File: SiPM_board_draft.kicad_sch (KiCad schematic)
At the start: 45 parts, among them J1 Conn_01x01_Pin, J10 Conn_01x01_Pin, J11 Conn_01x01_Pin, J12 Conn_01x01_Pin, J13 Conn_01x01_Pin, J14 Conn_01x01_Pin, J15 Conn_01x01_Pin, J16 Conn_01x01_Pin, J17 Conn_01x01_Pin, J18 Conn_01x01_Pin, J19 Conn_01x01_Pin, J2 Conn_01x01_Pin, J20 Conn_01x01_Pin, J21 Conn_01x01_Pin, J22 Conn_01x01_Pin, J23 Conn_01x01_Pin, J24 Conn_01x01_Pin, J25 Conn_01x01_Pin, J26 Conn_01x01_Pin, J27 Conn_01x01_Pin, J28 Conn_01x01_Pin, J29 Conn_01x01_Pin, J3 Conn_01x01_Pin, J30 Conn_01x01_Pin, J31 Conn_01x01_Pin, J32 Conn_01x01_Pin, J4 Conn_01x01_Pin, J5 Conn_01x01_Pin, J6 Conn_01x01_Pin, J7 Conn_01x01_Pin, J8 Conn_01x01_Pin, J9 Conn_01x01_Pin

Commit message: V1.0 submitted for fab
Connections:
- net A8: now also JP3.3 (B); no longer JP3.2 (C)
- net B3: now also JP2.3 (B); no longer JP2.2 (C)
- net C8: now also JP3.2 (C); no longer JP3.3 (B)
- net D1: now also JP2.2 (C); no longer JP2.3 (B)
- net E1: now also JP5.2 (C); no longer JP5.1 (A)
- net F8: now also JP8.2 (C); no longer JP8.1 (A)
- net G1: now also JP5.1 (A); no longer JP5.2 (C)
- net G5: now also JP7.2 (C); no longer JP7.3 (B)
- net G7: now also JP7.3 (B); no longer JP7.2 (C)
- net H2: now also JP6.3 (B); no longer JP6.2 (C)
- net H4: now also JP6.2 (C); no longer JP6.3 (B)
- net H8: now also JP8.1 (A); no longer JP8.2 (C)
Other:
- note added: "A1+A2+B2"
- note added: "A3+A4+B4"
- note added: "C1+D1+D2"
- note added: "Cable to SiPM connections"
- note added: "D3+D4+C4"
- note added: "SiPM part number: S14161-6050HS-04 Datasheet: https://www.hamamatsu.com/content/dam/hamamatsu-photonics/sites/documents/99_SALES_LIBRARY/ssd/s14160_s14161_series_kapd1064e.pdf"
- note added: "SiPM pinout"
- note added: "SiPM: pinout & ganged channels"
- note added: "Unplated throug-holes for mounting"
- company: (none) -> Lawrence Berkeley National Laboratory
- title: (none) -> QuIPS SiPM breakout board
- moved on the sheet: H1, H2, H3, H4, U1

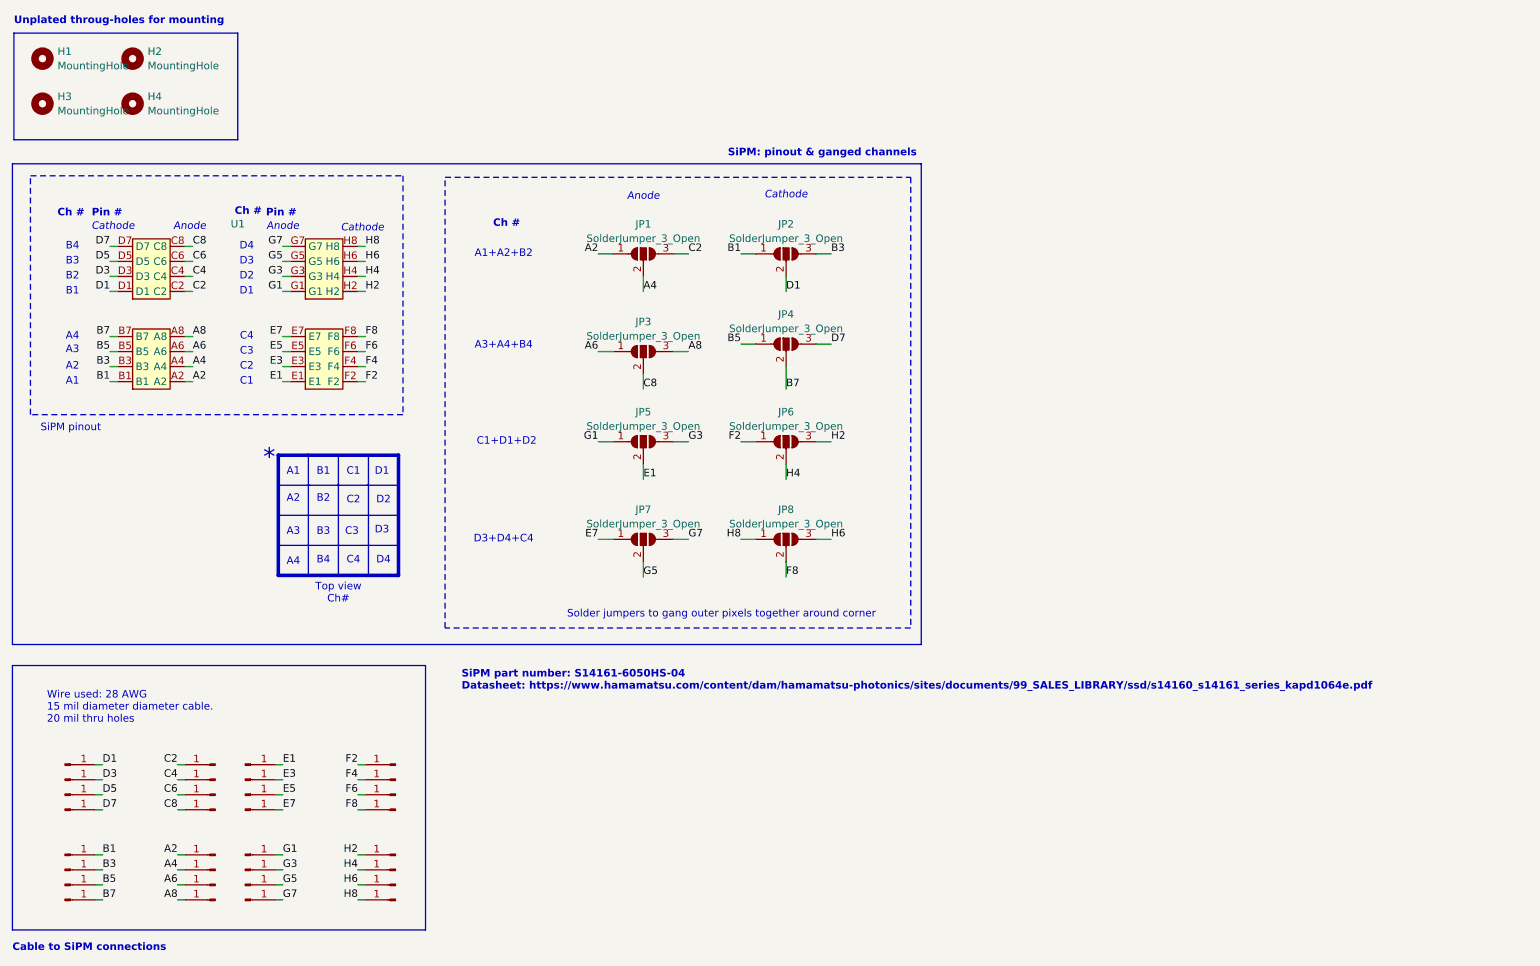
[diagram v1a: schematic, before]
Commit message: First draft of schematic for RC variant of board complete. Started placing with 0402 resistors and 1210 caps. Caps are really big. See if I can go smaller?
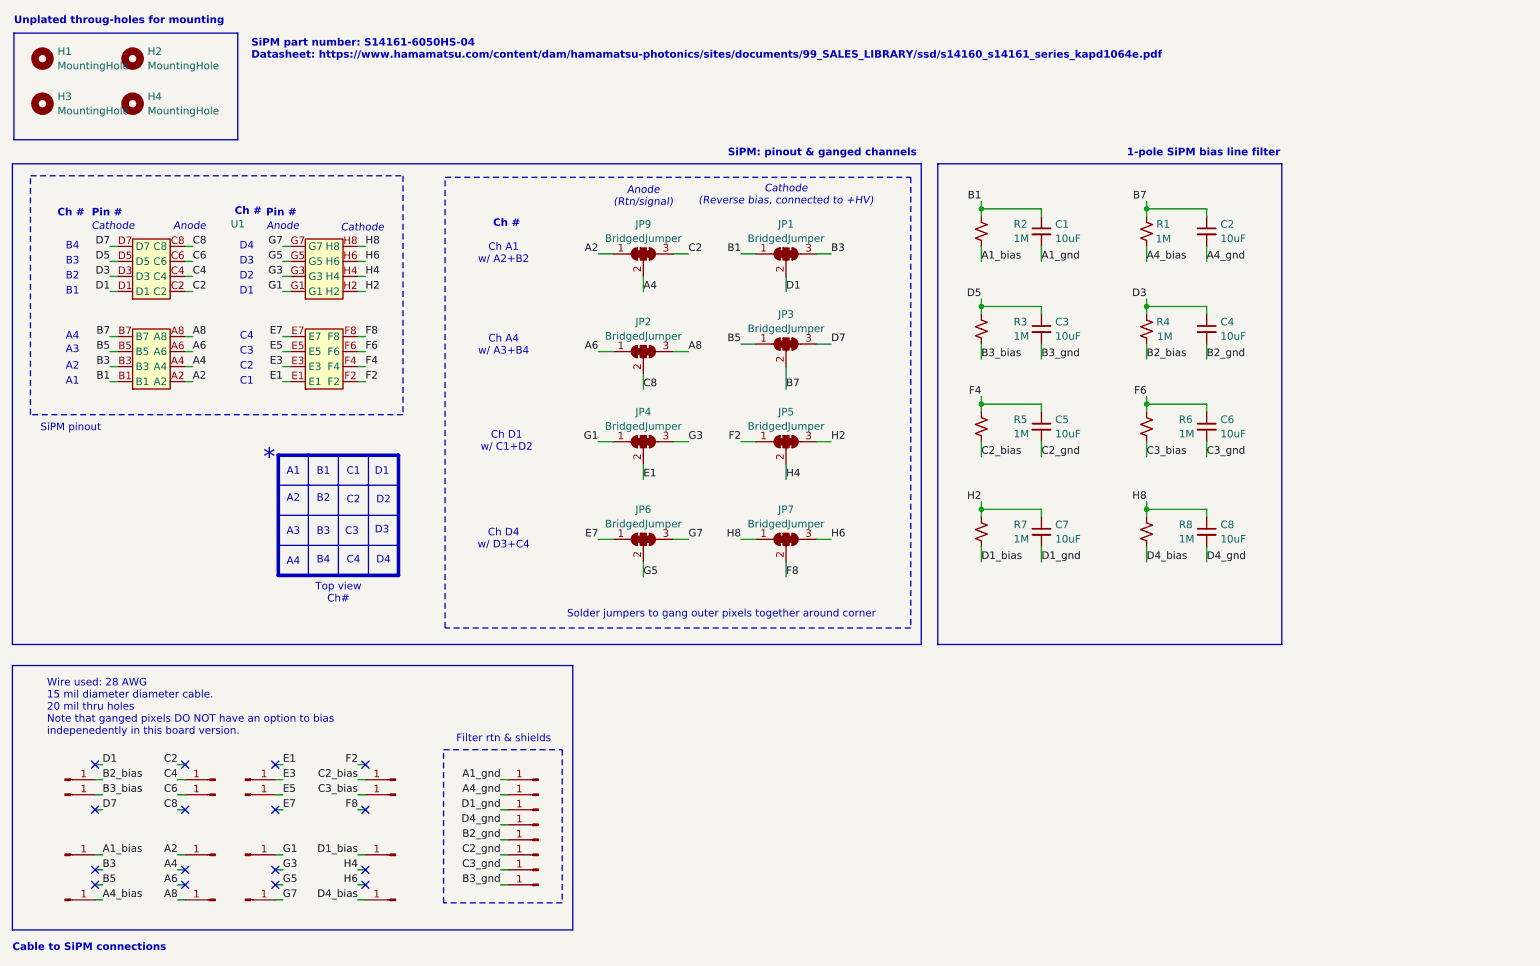
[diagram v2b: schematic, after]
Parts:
- removed J17, J20, J22, J23, J25, J28, J30, J31: Conn_01x01_Pin, Connector_Wire:SolderWire-0.15sqmm_1x01_D0.5mm_OD1.5mm, symbol Connector:Conn_01x01_Pin
- removed JP1, JP2, JP3, JP4, JP5, JP6, JP7, JP8: SolderJumper_3_Open, Jumper:SolderJumper-3_P2.0mm_Open_TrianglePad1.0x1.5mm, symbol Jumper:SolderJumper_3_Open
- added C1, C2, C3, C4, C5, C6, C7, C8: 10uF, Capacitor_SMD:C_1210_3225Metric, symbol Device:C_Small
- added JP1, JP2, JP3, JP4, JP5, JP6, JP7, JP9: BridgedJumper, symbol Jumper:SolderJumper_3_Bridged123
- added R1, R2, R3, R4, R5, R6, R7, R8: 1M, Resistor_SMD:R_0402_1005Metric, symbol Device:R_Small_US
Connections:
- net A2: now also JP9.1 (A)
- net A4: now also JP9.2 (C)
- net A6: now also JP2.1 (A)
- net A8: now also JP2.3 (B)
- net B1: now also C1.1, JP1.1 (A), R2.1; no longer J5.1 (Pin_1)
- net B3: now also JP1.3 (B); no longer J6.1 (Pin_1)
- net B5: now also JP3.1 (A); no longer J7.1 (Pin_1)
- net B7: now also C2.1, JP3.2 (C), R1.1; no longer J8.1 (Pin_1)
- net C2: now also JP9.3 (B)
- net C8: now also JP2.2 (C)
- net D1: now also JP1.2 (C); no longer J1.1 (Pin_1)
- net D3: now also C4.1, R4.1; no longer J2.1 (Pin_1)
- net D5: now also C3.1, R3.1; no longer J3.1 (Pin_1)
- net D7: now also JP3.3 (B); no longer J4.1 (Pin_1)
- net E1: now also JP4.2 (C); no longer J9.1 (Pin_1)
- net E7: now also JP6.1 (A); no longer J12.1 (Pin_1)
- net F2: now also JP5.1 (A)
- net F4: now also C5.1, R5.1; no longer J27.1 (Pin_1)
- net F6: now also C6.1, R6.1; no longer J26.1 (Pin_1)
- net F8: now also JP7.2 (C)
- net G1: now also JP4.1 (A)
- net G3: now also JP4.3 (B); no longer J14.1 (Pin_1)
- net G5: now also JP6.2 (C); no longer J15.1 (Pin_1)
- net G7: now also JP6.3 (B)
- net H2: now also C7.1, JP5.3 (B), R7.1; no longer J32.1 (Pin_1)
- net H4: now also JP5.2 (C)
- net H6: now also JP7.3 (B)
- net H8: now also C8.1, JP7.1 (A), R8.1; no longer J29.1 (Pin_1)
- new net A1_bias: J5.1 (Pin_1), R2.2
- new net A1_gnd: C1.2, J1.1 (Pin_1)
- new net A4_bias: J8.1 (Pin_1), R1.2
- new net A4_gnd: C2.2, J4.1 (Pin_1)
- new net B2_bias: J2.1 (Pin_1), R4.2
- new net B2_gnd: C4.2, J9.1 (Pin_1)
- new net B3_bias: J3.1 (Pin_1), R3.2
- new net B3_gnd: C3.2, J15.1 (Pin_1)
- new net C2_bias: J27.1 (Pin_1), R5.2
- new net C2_gnd: C5.2, J12.1 (Pin_1)
- new net C3_bias: J26.1 (Pin_1), R6.2
- new net C3_gnd: C6.2, J14.1 (Pin_1)
- new net D1_bias: J32.1 (Pin_1), R7.2
- new net D1_gnd: C7.2, J6.1 (Pin_1)
- new net D4_bias: J29.1 (Pin_1), R8.2
- new net D4_gnd: C8.2, J7.1 (Pin_1)
- no-connect marks 0 -> 16
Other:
- note added: "1-pole SiPM bias line filter"
- note added: "Anode (Rtn/signal)"
- note added: "Cathode (Reverse bias, connected to +HV)"
- note added: "Ch A1 w/ A2+B2"
- note added: "Ch A4 w/ A3+B4"
- note added: "Ch D1 w/ C1+D2"
- note added: "Ch D4 w/ D3+C4"
- note added: "Filter rtn & shields"
- note added: "Wire used: 28 AWG 15 mil diameter diameter cable. 20 mil thru holes Note that ganged pixels DO NOT have an option to bias indepenedently in this board version."
- note removed: "A1+A2+B2"
- note removed: "A3+A4+B4"
- note removed: "C1+D1+D2"
- note removed: "D3+D4+C4"
- note removed: "Wire used: 28 AWG 15 mil diameter diameter cable. 20 mil thru holes"

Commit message: Rough placement.
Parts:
- JP1, JP2, JP3, JP4, JP5, JP6, JP7, JP9: footprint (none) -> Jumper:SolderJumper-3_P1.3mm_Bridged123_Pad1.0x1.5mm
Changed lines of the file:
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@@
 			)
 		)
-		(property "Footprint" ""
+		(property "Footprint" "Jumper:SolderJumper-3_P1.3mm_Bridged123_Pad1.0x1.5mm"
 			(at 158.75 88.9 0)
 			(effects
@@
 			)
 		)
-		(property "Footprint" ""
+		(property "Footprint" "Jumper:SolderJumper-3_P1.3mm_Bridged123_Pad1.0x1.5mm"
 			(at 158.75 73.66 0)
 			(effects
@@
 			)
 		)
-		(property "Footprint" ""
+		(property "Footprint" "Jumper:SolderJumper-3_P1.3mm_Bridged123_Pad1.0x1.5mm"
 			(at 134.62 121.92 0)
 			(effects
@@
 			)
 		)
-		(property "Footprint" ""
+		(property "Footprint" "Jumper:SolderJumper-3_P1.3mm_Bridged123_Pad1.0x1.5mm"
 			(at 158.75 121.92 0)
 			(effects
@@
 			)
 		)
-		(property "Footprint" ""
+		(property "Footprint" "Jumper:SolderJumper-3_P1.3mm_Bridged123_Pad1.0x1.5mm"
 			(at 134.62 90.17 0)
 			(effects
@@
 			)
 		)
-		(property "Footprint" ""
+		(property "Footprint" "Jumper:SolderJumper-3_P1.3mm_Bridged123_Pad1.0x1.5mm"
 			(at 134.62 73.66 0)
 			(effects
@@
 			)
 		)
-		(property "Footprint" ""
+		(property "Footprint" "Jumper:SolderJumper-3_P1.3mm_Bridged123_Pad1.0x1.5mm"
 			(at 134.62 105.41 0)
 			(effects
@@
 			)
 		)
-		(property "Footprint" ""
+		(property "Footprint" "Jumper:SolderJumper-3_P1.3mm_Bridged123_Pad1.0x1.5mm"
 			(at 158.75 105.41 0)
 			(effects

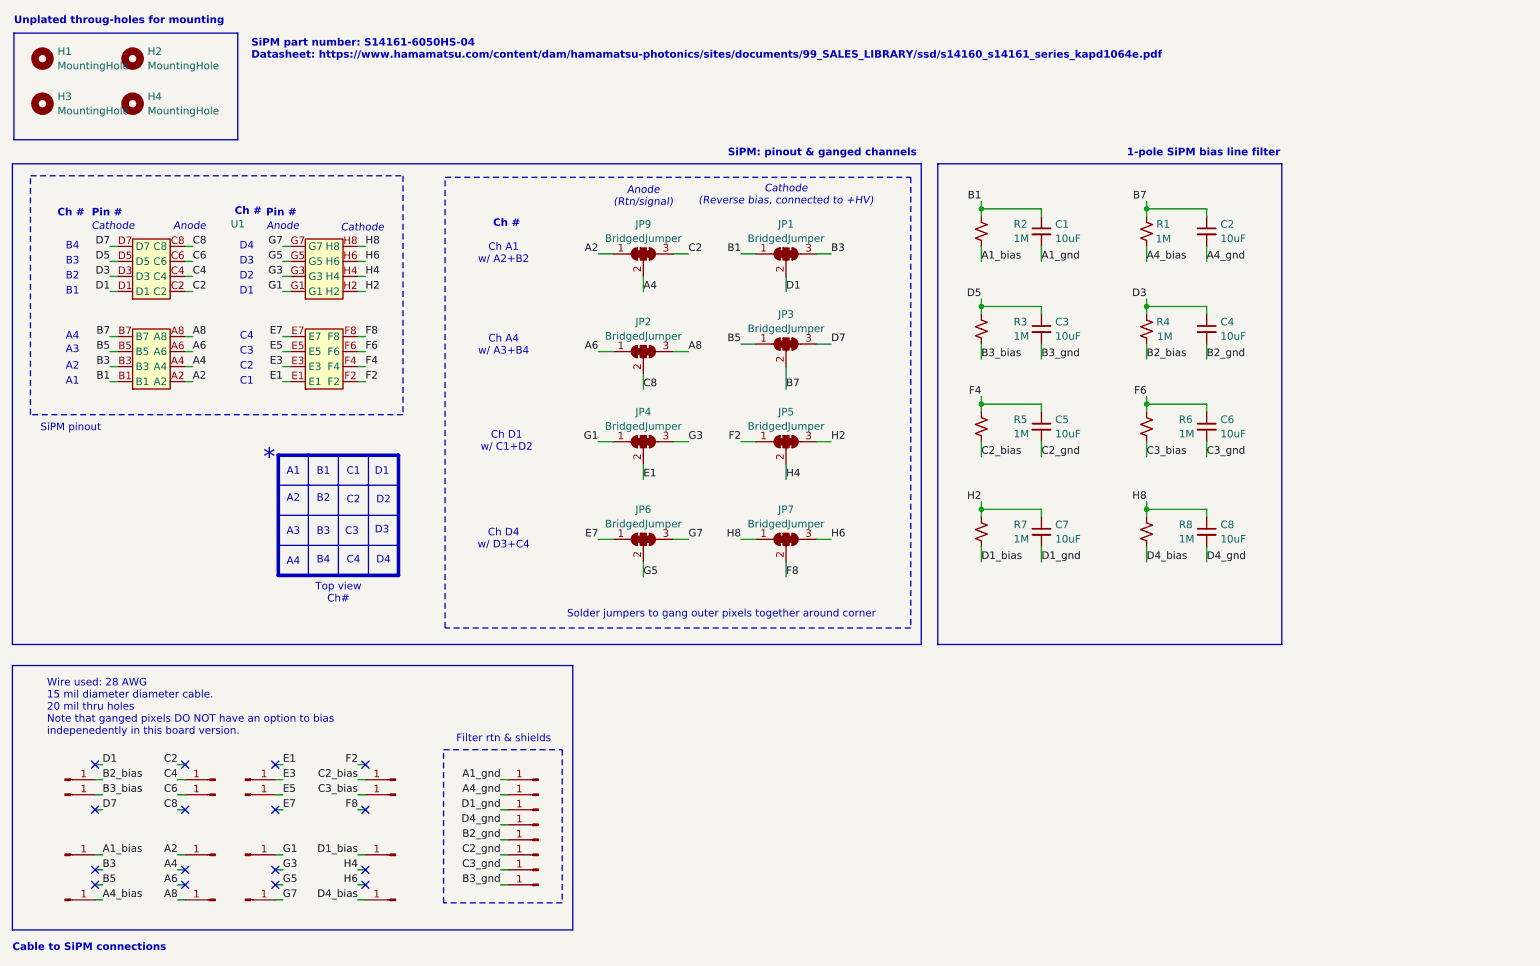
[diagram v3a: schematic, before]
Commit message: Changed everything to a common ground. Got rid of the jumpers and just made common nets. Reduced the number of ground lines on the board to 4. Everything placed. Going to try routing.
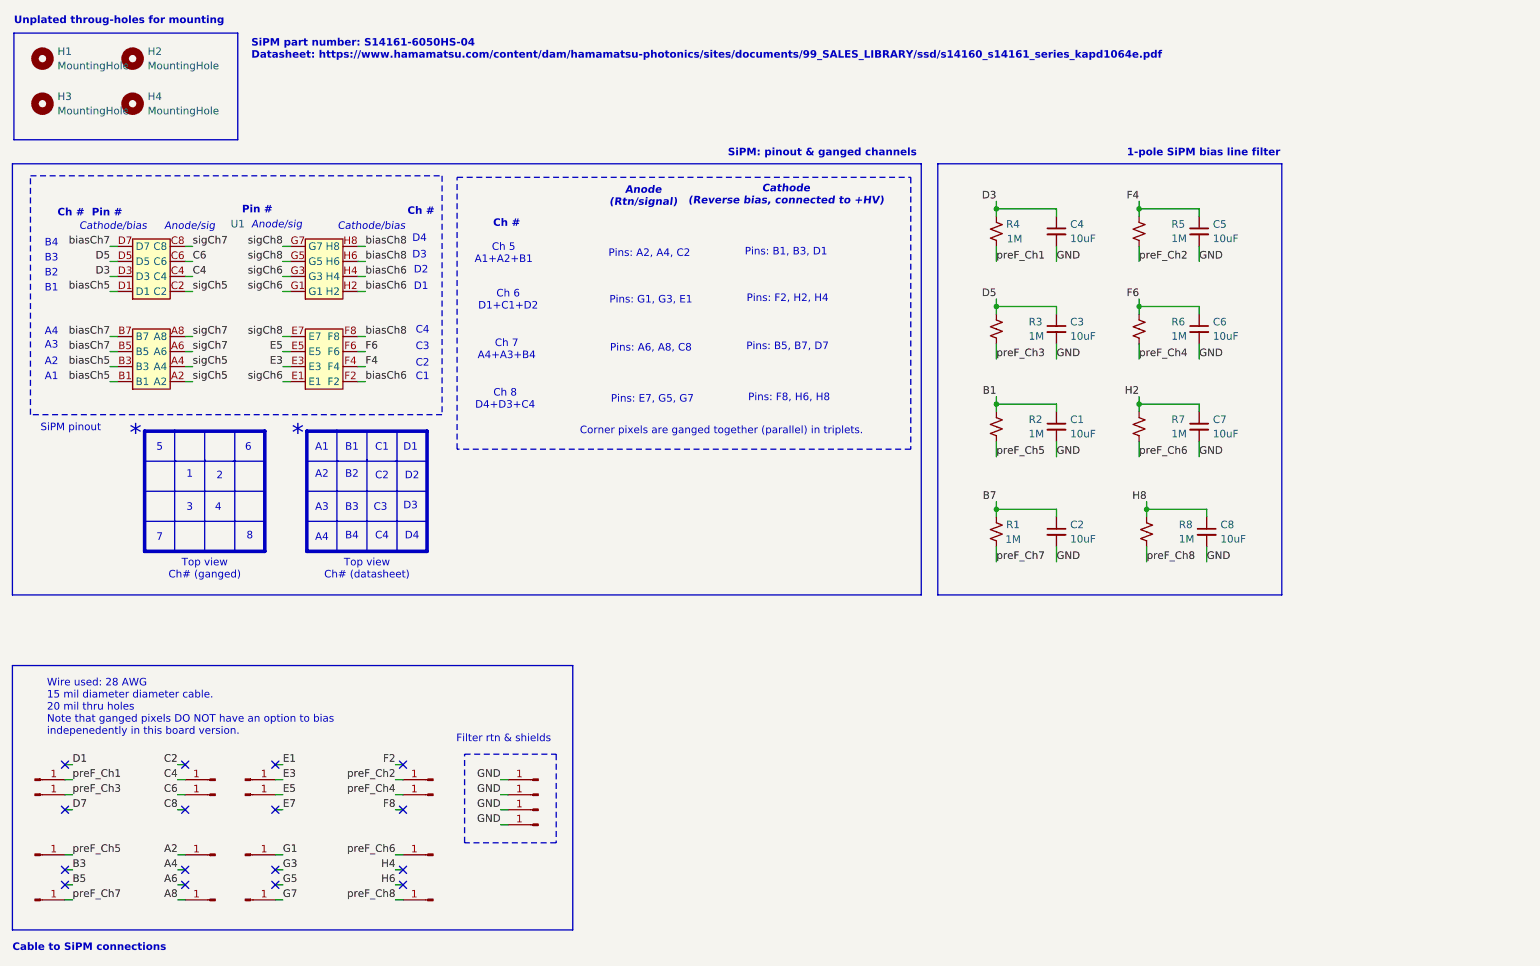
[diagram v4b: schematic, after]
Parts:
- removed J14, J15, J6, J9: Conn_01x01_Pin, Connector_Wire:SolderWire-0.15sqmm_1x01_D0.5mm_OD1.5mm, symbol Connector:Conn_01x01_Pin
- removed JP1, JP2, JP3, JP4, JP5, JP6, JP7, JP9: BridgedJumper, Jumper:SolderJumper-3_P1.3mm_Bridged123_Pad1.0x1.5mm, symbol Jumper:SolderJumper_3_Bridged123
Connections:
- net A4_gnd is gone; now on net GND: C2.2, J4.1 (Pin_1)
- net B2_gnd is gone; now on net GND: C4.2
- net B3_gnd is gone; now on net GND: C3.2
- net C2_gnd is gone; now on net GND: C5.2, J12.1 (Pin_1)
- net C3_gnd is gone; now on net GND: C6.2
- net D1_gnd is gone; now on net GND: C7.2
- net D4_gnd is gone; now on net GND: C8.2, J7.1 (Pin_1)
- net A2: no longer U1.A2
- net A4: no longer U1.A4
- net A6: no longer U1.A6
- net A8: no longer U1.A8
- net B1: no longer U1.B1
- net B3: no longer U1.B3
- net B5: no longer U1.B5
- net B7: no longer U1.B7
- net C2: no longer U1.C2
- net C8: no longer U1.C8
- net D1: no longer U1.D1
- net D7: no longer U1.D7
- net E1: no longer U1.E1
- net E7: no longer U1.E7
- net F2: no longer U1.F2
- net F8: no longer U1.F8
- net G1: no longer U1.G1
- net G3: no longer U1.G3
- net G5: no longer U1.G5
- net G7: no longer U1.G7
- net H2: no longer U1.H2
- net H4: no longer U1.H4
- net H6: no longer U1.H6
- net H8: no longer U1.H8
- net A1_bias renamed preF_Ch5
- net A1_gnd renamed GND
- net A4_bias renamed preF_Ch7
- net B2_bias renamed preF_Ch1
- net B3_bias renamed preF_Ch3
- net C2_bias renamed preF_Ch2
- net C3_bias renamed preF_Ch4
- net D1_bias renamed preF_Ch6
- net D4_bias renamed preF_Ch8
- new net biasCh5: U1.B1, U1.B3, U1.D1
- new net biasCh6: U1.F2, U1.H2, U1.H4
- new net biasCh7: U1.B5, U1.B7, U1.D7
- new net biasCh8: U1.F8, U1.H6, U1.H8
- new net sigCh5: U1.A2, U1.A4, U1.C2
- new net sigCh6: U1.E1, U1.G1, U1.G3
- new net sigCh7: U1.A6, U1.A8, U1.C8
- new net sigCh8: U1.E7, U1.G5, U1.G7
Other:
- note added: "1"
- note added: "2"
- note added: "3"
- note added: "4"
- note added: "5"
- note added: "6"
- note added: "7"
- note added: "8"
- note added: "Anode/sig"
- note added: "Cathode/bias"
- note added: "Ch 5 A1+A2+B1"
- note added: "Ch 6 D1+C1+D2"
- note added: "Ch 7 A4+A3+B4"
- note added: "Ch 8 D4+D3+C4"
- note added: "Corner pixels are ganged together (parallel) in triplets."
- note added: "Pins: A2, A4, C2"
- note added: "Pins: A6, A8, C8"
- note added: "Pins: B1, B3, D1"
- note added: "Pins: B5, B7, D7"
- note added: "Pins: E7, G5, G7"
- note added: "Pins: F2, H2, H4"
- note added: "Pins: F8, H6, H8"
- note added: "Pins: G1, G3, E1"
- note added: "Top view Ch# (datasheet)"
- note added: "Top view Ch# (ganged)"
- note removed: "Anode"
- note removed: "Cathode"
- note removed: "Ch A1 w/ A2+B2"
- note removed: "Ch A4 w/ A3+B4"
- note removed: "Ch D1 w/ C1+D2"
- note removed: "Ch D4 w/ D3+C4"
- note removed: "Solder jumpers to gang outer pixels together around corner"
- note removed: "Top view Ch#"
- moved on the sheet: C1, C2, C3, C4, C5, C6, C7, R1, R2, R3, R4, R5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
